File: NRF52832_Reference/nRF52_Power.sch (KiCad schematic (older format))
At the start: 28 parts

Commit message: Added LCD with SPI interface to schematic.
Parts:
- added C?: 4.7uF, symbol Device:C
- added C?: 1uF, symbol Device:C
- added SW?: SW_SPST, symbol Switch:SW_SPST
- added U?: AP2138N-3.0TRG1, symbol Project_Libary:AP2138N-3.0TRG1
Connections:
- net 5V: now also C?.1, U?.3 (IN)
- net GND: now also C?.2, C?.2, C?.2, U?.1 (GND)
- net V+: now also SW?.2 (B); no longer J?.2 (Pin_2), U?.5 (BAT), U?.5 (VCC)
- new net: J?.2 (Pin_2), SW?.1 (A), U?.5 (BAT), U?.5 (VCC)
- new net 3V: C?.1, U?.2 (OUT)
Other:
- moved on the sheet: C?, U?
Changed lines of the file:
@@
 L Device:C C?
 U 1 1 5BF5917C
-P 5400 5800
+P 1500 7075
 AR Path="/5BF5917C" Ref="C?"  Part="1"
 AR Path="/5BF31556/5BF5917C" Ref="C?"  Part="1"
-F 0 "C?" H 5150 5850 50  0000 L CNN
-F 1 "4.7uF" H 5075 5725 50  0000 L CNN
-F 2 "" H 5438 5650 50  0001 C CNN
-F 3 "~" H 5400 5800 50  0001 C CNN
-	1    5400 5800
+F 0 "C?" H 1250 7125 50  0000 L CNN
+F 1 "4.7uF" H 1175 7000 50  0000 L CNN
+F 2 "" H 1538 6925 50  0001 C CNN
+F 3 "~" H 1500 7075 50  0001 C CNN
+	1    1500 7075
 	1    0    0    -1
 $EndComp
@@
 L power:GND #PWR?
 U 1 1 5BF5918A
-P 5825 6100
+P 1925 7375
 AR Path="/5BF5918A" Ref="#PWR?"  Part="1"
 AR Path="/5BF31556/5BF5918A" Ref="#PWR?"  Part="1"
-F 0 "#PWR?" H 5825 5850 50  0001 C CNN
-F 1 "GND" H 5830 5927 50  0000 C CNN
-F 2 "" H 5825 6100 50  0001 C CNN
-F 3 "" H 5825 6100 50  0001 C CNN
-	1    5825 6100
+F 0 "#PWR?" H 1925 7125 50  0001 C CNN
+F 1 "GND" H 1930 7202 50  0000 C CNN
+F 2 "" H 1925 7375 50  0001 C CNN
+F 3 "" H 1925 7375 50  0001 C CNN
+	1    1925 7375
 	1    0    0    -1
 $EndComp
@@
 	0    1    1    0
 $EndComp
-Text Label 5500 2150 0    50   ~ 0
+Text Label 6200 2150 0    50   ~ 0
 V+
 Text Label 700  4900 0    50   ~ 0
@@
 Wire Wire Line
 	2400 4650 2400 4450
-Text HLabel 6675 5650 2    50   Output ~ 0
+Text HLabel 2775 6925 2    50   Output ~ 0
 3V3
 Text HLabel 5400 5100 2    50   Output ~ 0
@@
 L Device:C C?
 U 1 1 5BF59183
-P 6225 5800
+P 2325 7075
 AR Path="/5BF59183" Ref="C?"  Part="1"
 AR Path="/5BF31556/5BF59183" Ref="C?"  Part="1"
-F 0 "C?" H 6375 5875 50  0000 L CNN
-F 1 "4.7uF" H 6340 5755 50  0000 L CNN
-F 2 "" H 6263 5650 50  0001 C CNN
-F 3 "~" H 6225 5800 50  0001 C CNN
-	1    6225 5800
+F 0 "C?" H 2475 7150 50  0000 L CNN
+F 1 "4.7uF" H 2440 7030 50  0000 L CNN
+F 2 "" H 2363 6925 50  0001 C CNN
+F 3 "~" H 2325 7075 50  0001 C CNN
+	1    2325 7075
 	1    0    0    -1
 $EndComp
@@
 L Project_Libary:AP2114HA-3.3TRG1 U?
 U 1 1 5C0D7B49
-P 5825 5700
-F 0 "U?" H 5825 6015 50  0000 C CNN
-F 1 "AP2114HA-3.3TRG1" H 5825 5924 50  0000 C CNN
-F 2 "" H 5825 5950 50  0001 C CNN
-F 3 "" H 5825 5950 50  0001 C CNN
-	1    5825 5700
-	1    0    0    -1
-$EndComp
-Wire Wire Line
-	6225 5975 6225 6100
-Wire Wire Line
-	6225 6100 5825 6100
-Wire Wire Line
-	5400 5950 5400 6100
-Wire Wire Line
-	5400 6100 5825 6100
-Connection ~ 5825 6100
-Wire Wire Line
-	5825 6000 5825 6100
-Wire Wire Line
-	5525 5650 5400 5650
-Wire Wire Line
-	4975 5650 4975 5100
-Connection ~ 5400 5650
-Wire Wire Line
-	5400 5650 4975 5650
-Wire Wire Line
-	6125 5650 6225 5650
-Wire Wire Line
-	6225 5650 6675 5650
-Connection ~ 6225 5650
+P 1925 6975
+F 0 "U?" H 1925 7290 50  0000 C CNN
+F 1 "AP2114HA-3.3TRG1" H 1925 7199 50  0000 C CNN
+F 2 "" H 1925 7225 50  0001 C CNN
+F 3 "" H 1925 7225 50  0001 C CNN
+	1    1925 6975
+	1    0    0    -1
+$EndComp
+Wire Wire Line
+	2325 7375 1925 7375
+Wire Wire Line
+	1500 7225 1500 7375
+Wire Wire Line
+	1500 7375 1925 7375
+Connection ~ 1925 7375
+Wire Wire Line
+	1925 7275 1925 7375
+Wire Wire Line
+	1625 6925 1500 6925
+Connection ~ 1500 6925
+Wire Wire Line
+	1500 6925 1075 6925
+Wire Wire Line
+	2225 6925 2325 6925
+Wire Wire Line
+	2325 6925 2775 6925
+Connection ~ 2325 6925
 Wire Notes Line
 	7300 500  7300 6525
@@
 Wire Wire Line
 	3150 5950 3150 6000
+$Comp
+L Switch:SW_SPST SW?
+U 1 1 5C0B17BE
+P 5700 2150
+F 0 "SW?" H 5700 2385 50  0000 C CNN
+F 1 "SW_SPST" H 5700 2294 50  0000 C CNN
+F 2 "" H 5700 2150 50  0001 C CNN
+F 3 "" H 5700 2150 50  0001 C CNN
+	1    5700 2150
+	1    0    0    -1
+$EndComp
+Wire Wire Line
+	5900 2150 6200 2150
+Wire Wire Line
+	1075 6500 1075 6925
+Wire Wire Line
+	4975 5100 4975 6500
+$Comp
+L Project_Libary:AP2138N-3.0TRG1 U?
+U 1 1 5C11B1D5
+P 4025 6900
+F 0 "U?" H 4025 7165 50  0000 C CNN
+F 1 "AP2138N-3.0TRG1" H 4025 7074 50  0000 C CNN
+F 2 "" H 4025 7150 50  0001 C CNN
+F 3 "" H 4025 7150 50  0001 C CNN
+	1    4025 6900
+	1    0    0    -1
+$EndComp
+$Comp
+L Device:C C?
+U 1 1 5C11B374
+P 4475 7050
+AR Path="/5C11B374" Ref="C?"  Part="1"
+AR Path="/5BF31556/5C11B374" Ref="C?"  Part="1"
+F 0 "C?" H 4625 7125 50  0000 L CNN
+F 1 "4.7uF" H 4590 7005 50  0000 L CNN
+F 2 "" H 4513 6900 50  0001 C CNN
+F 3 "~" H 4475 7050 50  0001 C CNN
+	1    4475 7050
+	1    0    0    -1
+$EndComp
+Wire Wire Line
+	2325 7375 2325 7225
+$Comp
+L Device:C C?
+U 1 1 5C11E4AB
+P 3525 7050
+F 0 "C?" H 3640 7096 50  0000 L CNN
+F 1 "1uF" H 3640 7005 50  0000 L CNN
+F 2 "" H 3563 6900 50  0001 C CNN
+F 3 "~" H 3525 7050 50  0001 C CNN
+	1    3525 7050
+	1    0    0    -1
+$EndComp
+$Comp
+L power:GND #PWR?
+U 1 1 5C11E770
+P 4025 7375
+F 0 "#PWR?" H 4025 7125 50  0001 C CNN
+F 1 "GND" H 4030 7202 50  0000 C CNN
+F 2 "" H 4025 7375 50  0001 C CNN
+F 3 "" H 4025 7375 50  0001 C CNN
+	1    4025 7375
+	1    0    0    -1
+$EndComp
+Wire Wire Line
+	3525 7200 3525 7350
+Wire Wire Line
+	3525 7350 4025 7350
+Wire Wire Line
+	4025 7350 4025 7375
+Wire Wire Line
+	4025 7250 4025 7350
+Connection ~ 4025 7350
+Wire Wire Line
+	4475 7200 4475 7350
+Wire Wire Line
+	4475 7350 4025 7350
+Wire Wire Line
+	3725 6900 3525 6900
+Wire Wire Line
+	3325 6900 3325 6500
+Connection ~ 3525 6900
+Wire Wire Line
+	3525 6900 3325 6900
+Wire Wire Line
+	4325 6900 4475 6900
+Connection ~ 4475 6900
+Wire Wire Line
+	4475 6900 5150 6900
+Wire Wire Line
+	1075 6500 3325 6500
+Connection ~ 3325 6500
+Wire Wire Line
+	3325 6500 4975 6500
+Text HLabel 5150 6900 2    50   Input ~ 0
+3V
 $EndSCHEMATC

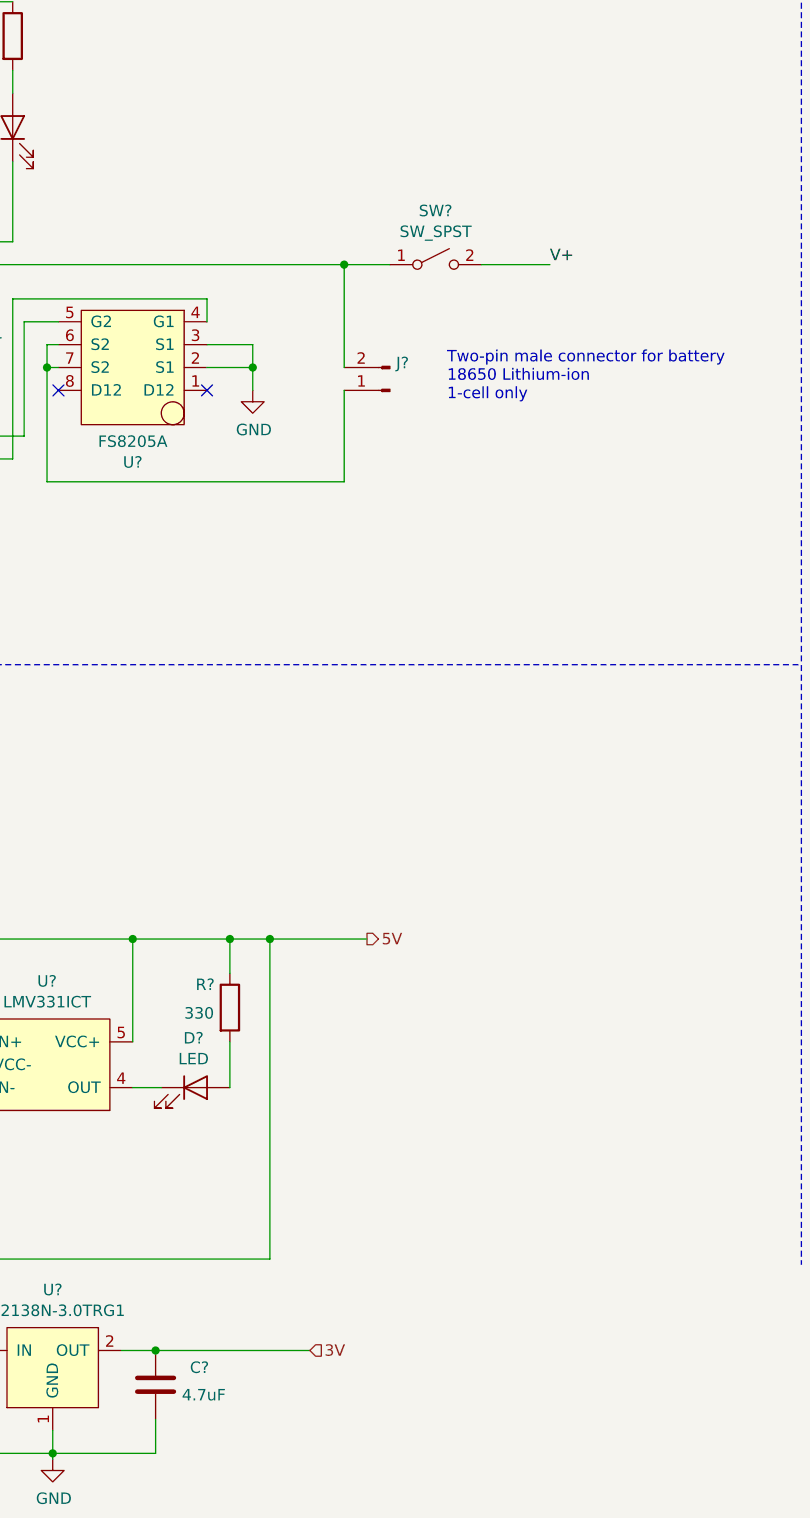
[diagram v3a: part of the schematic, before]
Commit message: Added main power switch and LCD power switch. Added GPIO breakout pins.
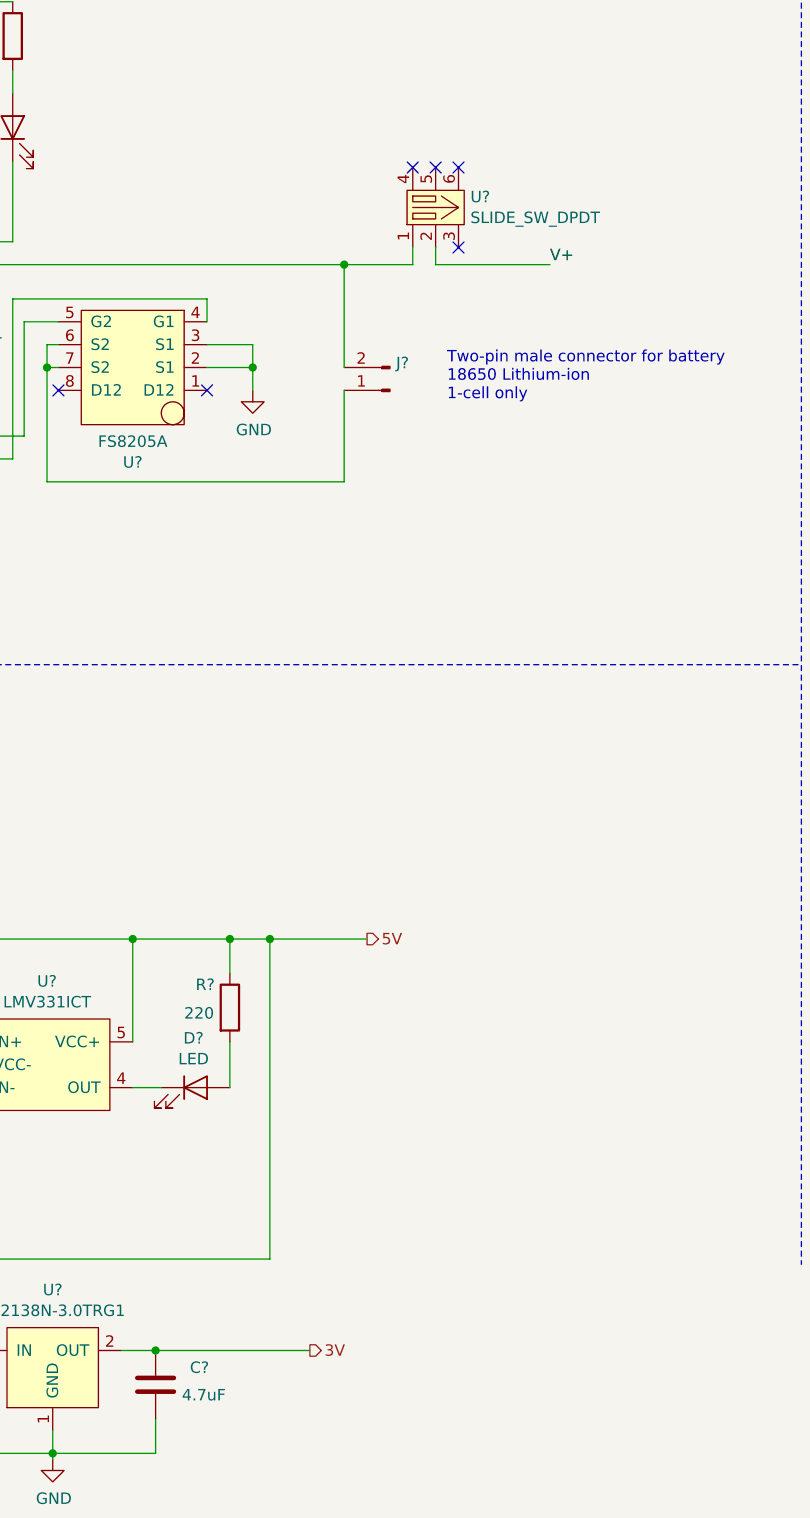
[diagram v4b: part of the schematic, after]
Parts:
- removed SW?: SW_SPST, symbol Switch:SW_SPST
- added U?: SLIDE_SW_DPDT, symbol Project_Libary:SLIDE_SW_DPDT
- R?: value 330 -> 220
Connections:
- net V+: now also U?.2
- net at J?.2 (Pin_2), U?.5 (BAT), U?.5 (VCC): now also U?.1
- no-connect marks 6 -> 10
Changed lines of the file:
@@
 NoConn ~ 4050 2700
 NoConn ~ 4700 2700
-Wire Wire Line
-	5500 2150 5300 2150
 Connection ~ 5300 2150
 $Comp
@@
 P 4800 5400
 F 0 "R?" H 4650 5500 50  0000 L CNN
-F 1 "330" H 4600 5375 50  0000 L CNN
+F 1 "220" H 4600 5375 50  0000 L CNN
 F 2 "" V 4730 5400 50  0001 C CNN
 F 3 "~" H 4800 5400 50  0001 C CNN
@@
 Wire Wire Line
 	2225 6925 2325 6925
-Wire Wire Line
-	2325 6925 2775 6925
 Connection ~ 2325 6925
 Wire Notes Line
@@
 Wire Wire Line
 	3150 5950 3150 6000
-$Comp
-L Switch:SW_SPST SW?
-U 1 1 5C0B17BE
-P 5700 2150
-F 0 "SW?" H 5700 2385 50  0000 C CNN
-F 1 "SW_SPST" H 5700 2294 50  0000 C CNN
-F 2 "" H 5700 2150 50  0001 C CNN
-F 3 "" H 5700 2150 50  0001 C CNN
-	1    5700 2150
-	1    0    0    -1
-$EndComp
-Wire Wire Line
-	5900 2150 6200 2150
 Wire Wire Line
 	1075 6500 1075 6925
@@
 Wire Wire Line
 	4475 6900 5150 6900
+Text HLabel 5150 6900 2    50   Output ~ 0
+3V
+$Comp
+L Project_Libary:SLIDE_SW_DPDT U?
+U 1 1 5C1C929E
+P 5700 1900
+F 0 "U?" H 5852 1946 50  0000 L CNN
+F 1 "SLIDE_SW_DPDT" H 5852 1855 50  0000 L CNN
+F 2 "" H 5700 2150 50  0001 C CNN
+F 3 "" H 5700 2150 50  0001 C CNN
+	1    5700 1900
+	1    0    0    -1
+$EndComp
+Wire Wire Line
+	5600 2150 5600 2075
+Wire Wire Line
+	5300 2150 5600 2150
+Wire Wire Line
+	5700 2150 5700 2075
+Wire Wire Line
+	5700 2150 6200 2150
+NoConn ~ 5800 2075
+NoConn ~ 5800 1725
+NoConn ~ 5700 1725
+NoConn ~ 5600 1725
+Wire Wire Line
+	2325 6925 2775 6925
+Connection ~ 3325 6500
+Wire Wire Line
+	3325 6500 4975 6500
 Wire Wire Line
 	1075 6500 3325 6500
-Connection ~ 3325 6500
-Wire Wire Line
-	3325 6500 4975 6500
-Text HLabel 5150 6900 2    50   Input ~ 0
-3V
 $EndSCHEMATC
